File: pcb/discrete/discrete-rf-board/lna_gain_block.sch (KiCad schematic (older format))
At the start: 21 parts, among them Q801 Q_NPN_BCEE

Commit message: The footprintening continues
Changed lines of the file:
@@
 $Descr A4 11693 8268
 encoding utf-8
-Sheet 14 19
+Sheet 16 19
 Title ""
 Date ""
@@
 AR Path="/5CA6B0AA/5CE74EBE/5D4104E7/5D3CF638" Ref="R903"  Part="1"
 AR Path="/5CA6B0AA/5CE74EBE/5D4124AC/5D3CF638" Ref="R1003"  Part="1"
-F 0 "R803" H 6041 3404 50  0000 R CNN
+F 0 "R1003" H 6041 3404 50  0000 R CNN
 F 1 "75R" H 6041 3495 50  0000 R CNN
 F 2 "" H 6100 3450 50  0001 C CNN
@@
 AR Path="/5CA6B0AA/5CE74EBE/5D4104E7/5D3CF640" Ref="C910"  Part="1"
 AR Path="/5CA6B0AA/5CE74EBE/5D4124AC/5D3CF640" Ref="C1010"  Part="1"
-F 0 "C810" V 7129 3250 50  0000 C CNN
+F 0 "C1010" V 7129 3250 50  0000 C CNN
 F 1 "100 pF RF" V 7038 3250 50  0000 C CNN
 F 2 "" H 6900 3250 50  0001 C CNN
@@
 AR Path="/5CA6B0AA/5CE74EBE/5D4104E7/5D3CF649" Ref="#PWR0903"  Part="1"
 AR Path="/5CA6B0AA/5CE74EBE/5D4124AC/5D3CF649" Ref="#PWR01003"  Part="1"
-F 0 "#PWR0803" H 4500 3800 50  0001 C CNN
+F 0 "#PWR01003" H 4500 3800 50  0001 C CNN
 F 1 "GND" H 4505 3877 50  0000 C CNN
 F 2 "" H 4500 4050 50  0001 C CNN
@@
 AR Path="/5CA6B0AA/5CE74EBE/5D4104E7/5D3CF650" Ref="#PWR0910"  Part="1"
 AR Path="/5CA6B0AA/5CE74EBE/5D4124AC/5D3CF650" Ref="#PWR01010"  Part="1"
-F 0 "#PWR0810" H 6700 3550 50  0001 C CNN
+F 0 "#PWR01010" H 6700 3550 50  0001 C CNN
 F 1 "GND" H 6705 3627 50  0000 C CNN
 F 2 "" H 6700 3800 50  0001 C CNN
@@
 AR Path="/5CA6B0AA/5CE74EBE/5D4104E7/5D3CF659" Ref="R901"  Part="1"
 AR Path="/5CA6B0AA/5CE74EBE/5D4124AC/5D3CF659" Ref="R1001"  Part="1"
-F 0 "R801" H 4441 3354 50  0000 R CNN
+F 0 "R1001" H 4441 3354 50  0000 R CNN
 F 1 "8k2R" H 4441 3445 50  0000 R CNN
 F 2 "" H 4500 3400 50  0001 C CNN
@@
 AR Path="/5CA6B0AA/5CE74EBE/5D4104E7/5D3CF668" Ref="C909"  Part="1"
 AR Path="/5CA6B0AA/5CE74EBE/5D4124AC/5D3CF668" Ref="C1009"  Part="1"
-F 0 "C809" H 6792 3696 50  0000 L CNN
+F 0 "C1009" H 6792 3696 50  0000 L CNN
 F 1 "3.0 pF RF" H 6792 3605 50  0000 L CNN
 F 2 "" H 6700 3650 50  0001 C CNN
@@
 AR Path="/5CA6B0AA/5CE74EBE/5D4104E7/5D3CF670" Ref="L903"  Part="1"
 AR Path="/5CA6B0AA/5CE74EBE/5D4124AC/5D3CF670" Ref="L1003"  Part="1"
-F 0 "L803" V 6485 3250 50  0000 C CNN
+F 0 "L1003" V 6485 3250 50  0000 C CNN
 F 1 "10.0 nH" V 6394 3250 50  0000 C CNN
 F 2 "" H 6300 3250 50  0001 C CNN
@@
 AR Path="/5CA6B0AA/5CE74EBE/5D4104E7/5D3CF693" Ref="C902"  Part="1"
 AR Path="/5CA6B0AA/5CE74EBE/5D4124AC/5D3CF693" Ref="C1002"  Part="1"
-F 0 "C802" V 4529 3700 50  0000 C CNN
+F 0 "C1002" V 4529 3700 50  0000 C CNN
 F 1 "100 pF RF" V 4438 3700 50  0000 C CNN
 F 2 "" H 4300 3700 50  0001 C CNN
@@
 AR Path="/5CA6B0AA/5CE74EBE/5D4104E7/5D3CF699" Ref="L901"  Part="1"
 AR Path="/5CA6B0AA/5CE74EBE/5D4124AC/5D3CF699" Ref="L1001"  Part="1"
-F 0 "L801" V 4885 3700 50  0000 C CNN
+F 0 "L1001" V 4885 3700 50  0000 C CNN
 F 1 "9.5 nH" V 4794 3700 50  0000 C CNN
 F 2 "" H 4700 3700 50  0001 C CNN
@@
 AR Path="/5CA6B0AA/5CE74EBE/5D4104E7/5D3CF69F" Ref="C904"  Part="1"
 AR Path="/5CA6B0AA/5CE74EBE/5D4124AC/5D3CF69F" Ref="C1004"  Part="1"
-F 0 "C804" H 4592 3946 50  0000 L CNN
+F 0 "C1004" H 4592 3946 50  0000 L CNN
 F 1 "5.45 pF RF" H 4592 3855 50  0000 L CNN
 F 2 "" H 4500 3900 50  0001 C CNN
@@
 AR Path="/5CA6B0AA/5CE74EBE/5D4104E7/5D3CF6A6" Ref="#PWR0909"  Part="1"
 AR Path="/5CA6B0AA/5CE74EBE/5D4124AC/5D3CF6A6" Ref="#PWR01009"  Part="1"
-F 0 "#PWR0809" H 5550 3950 50  0001 C CNN
+F 0 "#PWR01009" H 5550 3950 50  0001 C CNN
 F 1 "GND" H 5555 4027 50  0000 C CNN
 F 2 "" H 5550 4200 50  0001 C CNN
@@
 AR Path="/5CA6B0AA/5CE74EBE/5D4104E7/5D3E5B01" Ref="C903"  Part="1"
 AR Path="/5CA6B0AA/5CE74EBE/5D4124AC/5D3E5B01" Ref="C1003"  Part="1"
-F 0 "C803" H 4410 2620 50  0000 L CNN
+F 0 "C1003" H 4410 2620 50  0000 L CNN
 F 1 "1 nF" H 4410 2470 50  0000 L CNN
 F 2 "" H 4400 2550 50  0001 C CNN
@@
 AR Path="/5CA6B0AA/5CE74EBE/5D4104E7/5D3E5B07" Ref="C906"  Part="1"
 AR Path="/5CA6B0AA/5CE74EBE/5D4124AC/5D3E5B07" Ref="C1006"  Part="1"
-F 0 "C806" H 4810 2620 50  0000 L CNN
+F 0 "C1006" H 4810 2620 50  0000 L CNN
 F 1 "100 pF RF" H 4810 2470 50  0000 L CNN
 F 2 "" H 4800 2550 50  0001 C CNN
@@
 AR Path="/5CA6B0AA/5CE74EBE/5D4104E7/5D3E5B0D" Ref="C908"  Part="1"
 AR Path="/5CA6B0AA/5CE74EBE/5D4124AC/5D3E5B0D" Ref="C1008"  Part="1"
-F 0 "C808" H 5210 2620 50  0000 L CNN
+F 0 "C1008" H 5210 2620 50  0000 L CNN
 F 1 "100 pF RF" H 5210 2470 50  0000 L CNN
 F 2 "" H 5200 2550 50  0001 C CNN
@@
 AR Path="/5CA6B0AA/5CE74EBE/5D4104E7/5D3E5B13" Ref="#PWR0902"  Part="1"
 AR Path="/5CA6B0AA/5CE74EBE/5D4124AC/5D3E5B13" Ref="#PWR01002"  Part="1"
-F 0 "#PWR0802" H 4400 2500 50  0001 C CNN
+F 0 "#PWR01002" H 4400 2500 50  0001 C CNN
 F 1 "GND" H 4400 2600 50  0000 C CNN
 F 2 "" H 4400 2750 50  0001 C CNN
@@
 AR Path="/5CA6B0AA/5CE74EBE/5D4104E7/5D3E5B19" Ref="#PWR0905"  Part="1"
 AR Path="/5CA6B0AA/5CE74EBE/5D4124AC/5D3E5B19" Ref="#PWR01005"  Part="1"
-F 0 "#PWR0805" H 4800 2500 50  0001 C CNN
+F 0 "#PWR01005" H 4800 2500 50  0001 C CNN
 F 1 "GND" H 4800 2600 50  0000 C CNN
 F 2 "" H 4800 2750 50  0001 C CNN
@@
 AR Path="/5CA6B0AA/5CE74EBE/5D4104E7/5D3E5B1F" Ref="#PWR0908"  Part="1"
 AR Path="/5CA6B0AA/5CE74EBE/5D4124AC/5D3E5B1F" Ref="#PWR01008"  Part="1"
-F 0 "#PWR0808" H 5200 2500 50  0001 C CNN
+F 0 "#PWR01008" H 5200 2500 50  0001 C CNN
 F 1 "GND" H 5200 2600 50  0000 C CNN
 F 2 "" H 5200 2750 50  0001 C CNN
@@
 AR Path="/5CA6B0AA/5CE74EBE/5D4104E7/5D3E5B25" Ref="C907"  Part="1"
 AR Path="/5CA6B0AA/5CE74EBE/5D4124AC/5D3E5B25" Ref="C1007"  Part="1"
-F 0 "C807" H 5160 1920 50  0000 L CNN
+F 0 "C1007" H 5160 1920 50  0000 L CNN
 F 1 "100 pF RF" H 5160 1770 50  0000 L CNN
 F 2 "" H 5150 1850 50  0001 C CNN
@@
 AR Path="/5CA6B0AA/5CE74EBE/5D4104E7/5D3E5B2B" Ref="#PWR0907"  Part="1"
 AR Path="/5CA6B0AA/5CE74EBE/5D4124AC/5D3E5B2B" Ref="#PWR01007"  Part="1"
-F 0 "#PWR0807" H 5150 1800 50  0001 C CNN
+F 0 "#PWR01007" H 5150 1800 50  0001 C CNN
 F 1 "GND" H 5150 1900 50  0000 C CNN
 F 2 "" H 5150 2050 50  0001 C CNN
@@
 AR Path="/5CA6B0AA/5CE74EBE/5D4104E7/5D3E5B31" Ref="C905"  Part="1"
 AR Path="/5CA6B0AA/5CE74EBE/5D4124AC/5D3E5B31" Ref="C1005"  Part="1"
-F 0 "C805" H 4760 1920 50  0000 L CNN
+F 0 "C1005" H 4760 1920 50  0000 L CNN
 F 1 "1 nF" H 4760 1770 50  0000 L CNN
 F 2 "" H 4750 1850 50  0001 C CNN
@@
 AR Path="/5CA6B0AA/5CE74EBE/5D4104E7/5D3E5B37" Ref="#PWR0904"  Part="1"
 AR Path="/5CA6B0AA/5CE74EBE/5D4124AC/5D3E5B37" Ref="#PWR01004"  Part="1"
-F 0 "#PWR0804" H 4750 1800 50  0001 C CNN
+F 0 "#PWR01004" H 4750 1800 50  0001 C CNN
 F 1 "GND" H 4750 1900 50  0000 C CNN
 F 2 "" H 4750 2050 50  0001 C CNN
@@
 AR Path="/5CA6B0AA/5CE74EBE/5D4104E7/5D3F1C48" Ref="R904"  Part="1"
 AR Path="/5CA6B0AA/5CE74EBE/5D4124AC/5D3F1C48" Ref="R1004"  Part="1"
-F 0 "R804" H 5580 2120 50  0000 L CNN
+F 0 "R1004" H 5580 2120 50  0000 L CNN
 F 1 "22R" H 5580 2060 50  0000 L CNN
 F 2 "" H 5550 2100 50  0001 C CNN
@@
 AR Path="/5CA6B0AA/5CE74EBE/5D4104E7/5D3FEB6E" Ref="C901"  Part="1"
 AR Path="/5CA6B0AA/5CE74EBE/5D4124AC/5D3FEB6E" Ref="C1001"  Part="1"
-F 0 "C801" H 4010 2620 50  0000 L CNN
+F 0 "C1001" H 4010 2620 50  0000 L CNN
 F 1 "1 nF" H 4010 2470 50  0000 L CNN
 F 2 "" H 4000 2550 50  0001 C CNN
@@
 AR Path="/5CA6B0AA/5CE74EBE/5D4104E7/5D3FEB74" Ref="#PWR0901"  Part="1"
 AR Path="/5CA6B0AA/5CE74EBE/5D4124AC/5D3FEB74" Ref="#PWR01001"  Part="1"
-F 0 "#PWR0801" H 4000 2500 50  0001 C CNN
+F 0 "#PWR01001" H 4000 2500 50  0001 C CNN
 F 1 "GND" H 4000 2600 50  0000 C CNN
 F 2 "" H 4000 2750 50  0001 C CNN
@@
 AR Path="/5CA6B0AA/5CE74EBE/5D4104E7/5D40D244" Ref="L902"  Part="1"
 AR Path="/5CA6B0AA/5CE74EBE/5D4124AC/5D40D244" Ref="L1002"  Part="1"
-F 0 "L802" H 5580 3090 50  0000 L CNN
+F 0 "L1002" H 5580 3090 50  0000 L CNN
 F 1 "220 nH" H 5580 3010 50  0000 L CNN
 F 2 "" H 5550 3050 50  0001 C CNN
@@
 AR Path="/5CA6B0AA/5CE74EBE/5D4104E7/5D435867" Ref="R902"  Part="1"
 AR Path="/5CA6B0AA/5CE74EBE/5D4124AC/5D435867" Ref="R1002"  Part="1"
-F 0 "R802" H 4941 3254 50  0000 R CNN
+F 0 "R1002" H 4941 3254 50  0000 R CNN
 F 1 "1k8R" H 4941 3345 50  0000 R CNN
 F 2 "" H 5000 3300 50  0001 C CNN
@@
 AR Path="/5CA6B0AA/5CE74EBE/5D3C8D48/5D43681D" Ref="#PWR0806"  Part="1"
 AR Path="/5CA6B0AA/5CE74EBE/5D4104E7/5D43681D" Ref="#PWR0906"  Part="1"
-F 0 "#PWR0806" H 5000 3250 50  0001 C CNN
+F 0 "#PWR01006" H 5000 3250 50  0001 C CNN
 F 1 "GND" H 5000 3350 50  0000 C CNN
 F 2 "" H 5000 3500 50  0001 C CNN
@@
 AR Path="/5CA6B0AA/5CE74EBE/5D4104E7/5D191C23" Ref="Q901"  Part="1"
 AR Path="/5CA6B0AA/5CE74EBE/5D4124AC/5D191C23" Ref="Q1001"  Part="1"
-F 0 "Q801" H 5800 3700 50  0000 C CNN
+F 0 "Q1001" H 5800 3700 50  0000 C CNN
 F 1 "Q_NPN_BCEE" H 5700 3600 50  0000 L CNN
 F 2 "" H 5500 3700 50  0001 C CNN

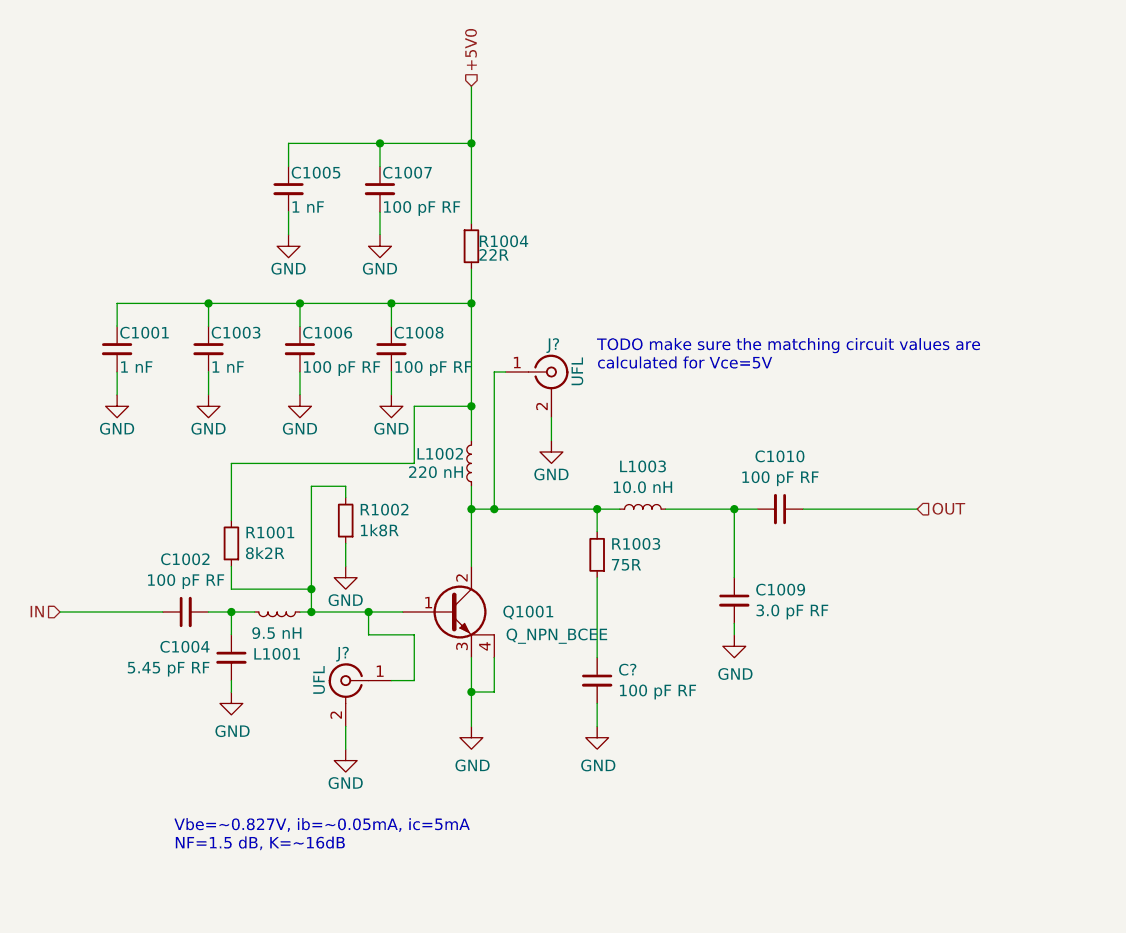
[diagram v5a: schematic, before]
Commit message: Add matching PNP/NPN transistor pairs, fix pin numbering for BFU520R transistors TODO fix biasing on power stage, source last NPN transistor, autofill and start sourcing passives
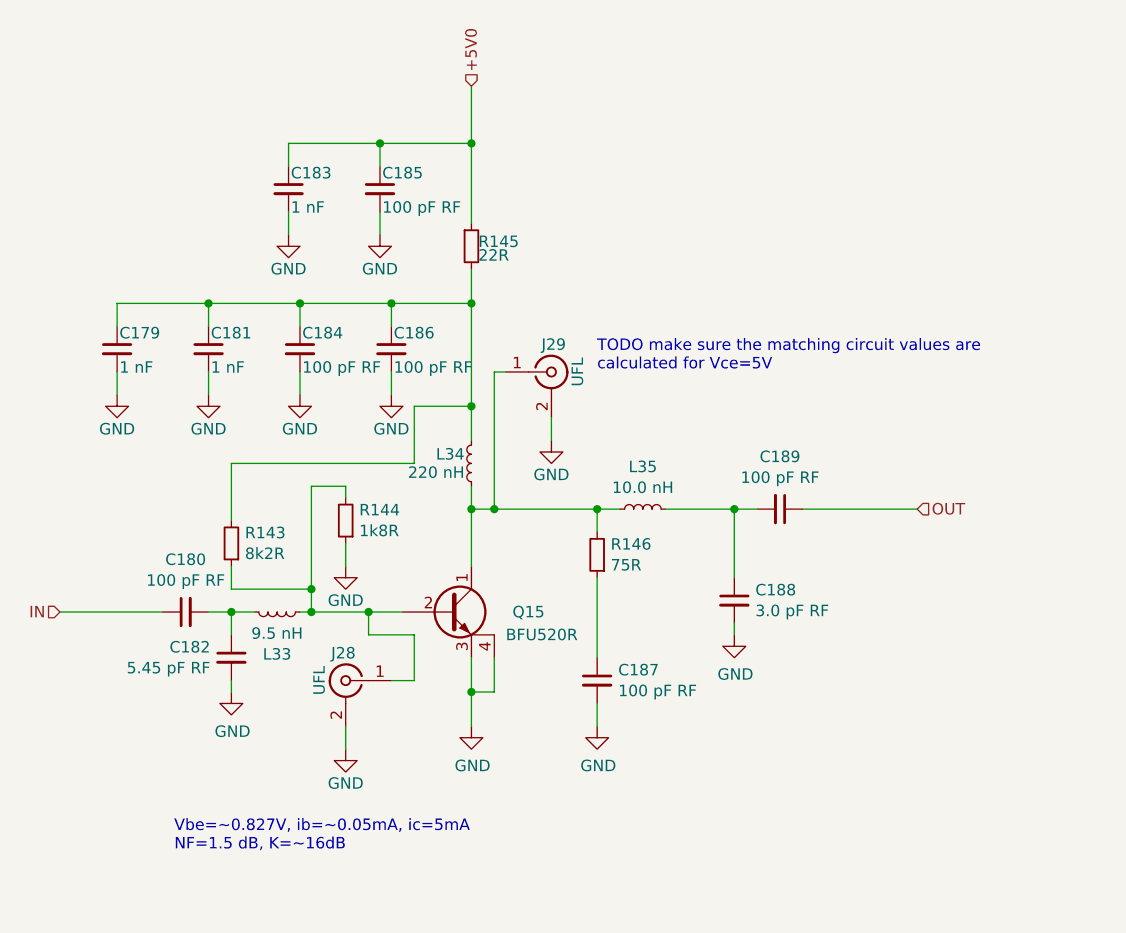
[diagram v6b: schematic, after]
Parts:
- removed Q801: Q_NPN_BCEE, symbol discrete-parts:Q_NPN_BCEE
- added Q15: BFU520R, symbol discrete-parts:Q_NPN_CBEE
- gave numbers to parts that had none: 3
- renumbered C801 to C157, C802 to C158, C803 to C159, C804 to C160, C805 to C161, C806 to C162, C807 to C163, C808 to C164, C809 to C166, C810 to C167, L801 to L27, L802 to L28, L803 to L29, R801 to R135, R802 to R136, R804 to R137, R803 to R138
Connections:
- net GND: now also Q15.3 (E), Q15.4 (C)
- net at J24.1 (In), L27.2, R135.1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: now also Q15.2 (B)
- net at J25.1 (In), L28.2, L29.1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: now also Q15.1 (C)

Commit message: All component values set (TODO change transistor gain stages to match values from experimentation
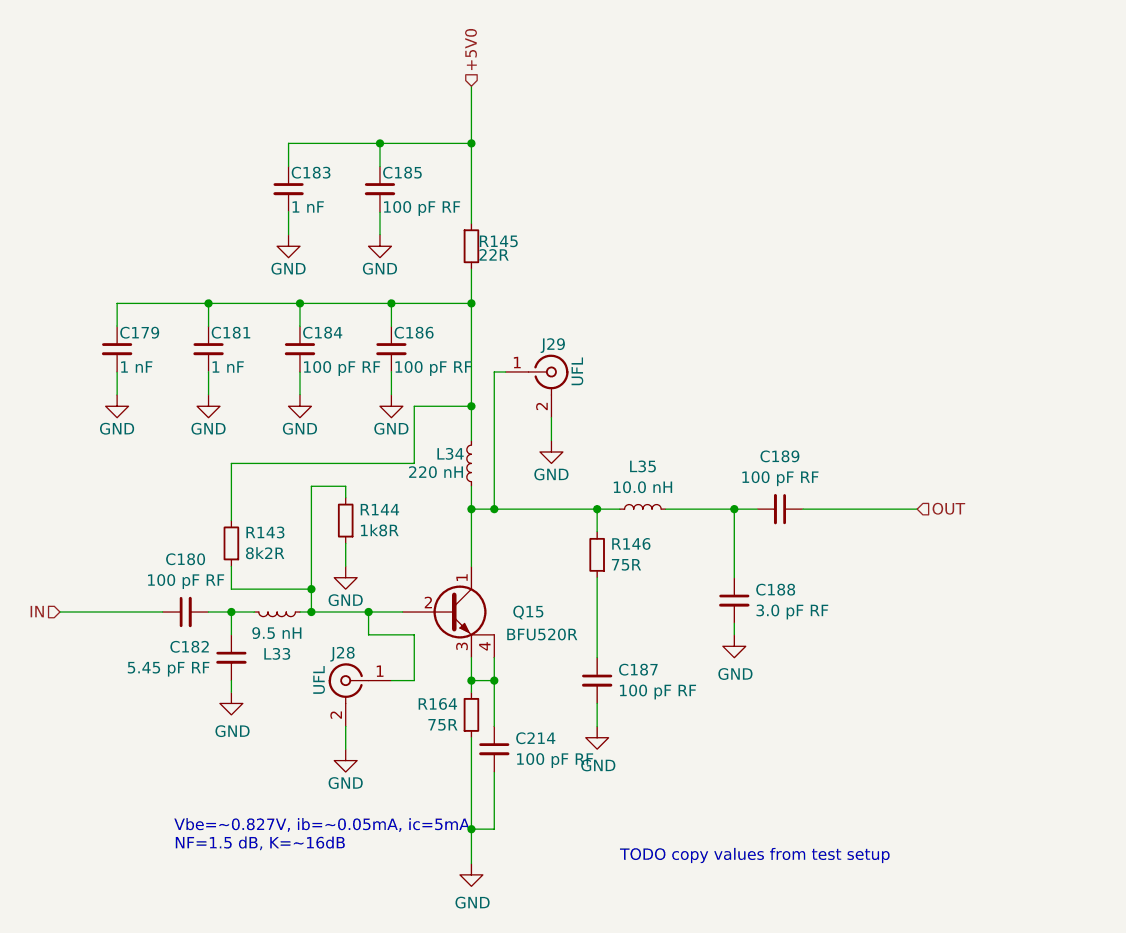
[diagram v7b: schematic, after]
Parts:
- added C212: 100 pF RF, symbol Device:C_Small
- added R162: 75R, symbol Device:R_Small
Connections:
- net GND: now also C212.2, R162.1; no longer Q15.3 (E), Q15.4 (C)
- new net: C212.1, Q15.3 (E), Q15.4 (C), R162.2
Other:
- note added: "TODO copy values from test setup"
- note removed: "TODO make sure the matching circuit values are\ncalculated for Vce=5V"
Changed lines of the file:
@@
 L power:GND #PWR?
 U 1 1 5D3CF6A6
-P 5550 4200
+P 5550 4800
 AR Path="/5CA6B0AA/5CE74EBE/5D3CF6A6" Ref="#PWR?"  Part="1"
 AR Path="/5CA6B0AA/5CE74EBE/5D3C8D48/5D3CF6A6" Ref="#PWR0208"  Part="1"
@@
 AR Path="/5CA6B0AA/5CE74EBE/5D4104E7/5D3CF6A6" Ref="#PWR0221"  Part="1"
 AR Path="/5CA6B0AA/5CE74EBE/5D4124AC/5D3CF6A6" Ref="#PWR0234"  Part="1"
-F 0 "#PWR0234" H 5550 3950 50  0001 C CNN
-F 1 "GND" H 5555 4027 50  0000 C CNN
-F 2 "" H 5550 4200 50  0001 C CNN
-F 3 "" H 5550 4200 50  0001 C CNN
-	1    5550 4200
+F 0 "#PWR0234" H 5550 4550 50  0001 C CNN
+F 1 "GND" H 5555 4627 50  0000 C CNN
+F 2 "" H 5550 4800 50  0001 C CNN
+F 3 "" H 5550 4800 50  0001 C CNN
+	1    5550 4800
 	1    0    0    -1
 $EndComp
@@
 	5000 3150 5000 3200
 Wire Wire Line
-	5550 3900 5550 4050
-Wire Wire Line
-	5650 3900 5650 4050
-Wire Wire Line
-	5650 4050 5550 4050
-Connection ~ 5550 4050
-Wire Wire Line
-	5550 4050 5550 4200
+	5650 4650 5550 4650
+Connection ~ 5550 4650
+Wire Wire Line
+	5550 4650 5550 4800
 Text Notes 4250 4750 0    50   ~ 0
 Vbe=~~0.827V, ib=~~0.05mA, ic=5mA\nNF=1.5 dB, K=~~16dB
-Text Notes 6100 2650 0    50   ~ 0
-TODO make sure the matching circuit values are\ncalculated for Vce=5V
 $Comp
 L Device:C_Small C?
@@
 	1    0    0    -1
 $EndComp
+Wire Wire Line
+	5550 3900 5550 4000
+Wire Wire Line
+	5550 4000 5650 4000
+Wire Wire Line
+	5650 4000 5650 3900
+$Comp
+L Device:C_Small C?
+U 1 1 5DAA0359
+P 5650 4300
+AR Path="/5CA6B0AA/5CE74EBE/5DAA0359" Ref="C?"  Part="1"
+AR Path="/5CA6B0AA/5CE74EBE/5D3C8D48/5DAA0359" Ref="C212"  Part="1"
+AR Path="/5CA6B0AA/5CE74EBE/5D407D69/5DAA0359" Ref="C?"  Part="1"
+AR Path="/5CA6B0AA/5CE74EBE/5D407DF5/5DAA0359" Ref="C?"  Part="1"
+AR Path="/5CA6B0AA/5CE74EBE/5D4104E7/5DAA0359" Ref="C213"  Part="1"
+AR Path="/5CA6B0AA/5CE74EBE/5D4124AC/5DAA0359" Ref="C214"  Part="1"
+F 0 "C214" H 5742 4346 50  0000 L CNN
+F 1 "100 pF RF" H 5742 4255 50  0000 L CNN
+F 2 "" H 5650 4300 50  0001 C CNN
+F 3 "~" H 5650 4300 50  0001 C CNN
+	1    5650 4300
+	1    0    0    -1
+$EndComp
+Wire Wire Line
+	5650 4400 5650 4650
+Wire Wire Line
+	5650 4200 5650 4000
+Connection ~ 5650 4000
+$Comp
+L Device:R_Small R?
+U 1 1 5DAA3BBB
+P 5550 4150
+AR Path="/5CA6B0AA/5CE74EBE/5DAA3BBB" Ref="R?"  Part="1"
+AR Path="/5CA6B0AA/5CE74EBE/5D3C8D48/5DAA3BBB" Ref="R162"  Part="1"
+AR Path="/5CA6B0AA/5CE74EBE/5D407D69/5DAA3BBB" Ref="R?"  Part="1"
+AR Path="/5CA6B0AA/5CE74EBE/5D407DF5/5DAA3BBB" Ref="R?"  Part="1"
+AR Path="/5CA6B0AA/5CE74EBE/5D4104E7/5DAA3BBB" Ref="R163"  Part="1"
+AR Path="/5CA6B0AA/5CE74EBE/5D4124AC/5DAA3BBB" Ref="R164"  Part="1"
+F 0 "R164" H 5491 4104 50  0000 R CNN
+F 1 "75R" H 5491 4195 50  0000 R CNN
+F 2 "" H 5550 4150 50  0001 C CNN
+F 3 "~" H 5550 4150 50  0001 C CNN
+	1    5550 4150
+	1    0    0    1
+$EndComp
+Wire Wire Line
+	5550 4250 5550 4650
+Wire Wire Line
+	5550 4050 5550 4000
+Connection ~ 5550 4000
+Text Notes 6200 4800 0    50   ~ 0
+TODO copy values from test setup
 $EndSCHEMATC

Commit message: Autofill; lots left to do
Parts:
- J24, J25: footprint (none) -> discrete_footprints:2337019-1; Mouser (none) -> 571-2337019-1
- Q15: footprint (none) -> discrete_footprints:NXP_SOT143B; Mouser (none) -> 771-BFU520R
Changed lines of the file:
@@
 F 0 "J29" H 5910 2770 50  0000 C CNN
 F 1 "UFL" V 6015 2650 50  0000 C CNN
-F 2 "" H 5900 2650 50  0001 C CNN
+F 2 "discrete_footprints:2337019-1" H 5900 2650 50  0001 C CNN
 F 3 " ~" H 5900 2650 50  0001 C CNN
+F 4 " 571-2337019-1" H 5900 2650 50  0001 C CNN "Mouser"
 	1    5900 2650
 	1    0    0    -1
@@
 F 0 "J28" H 5010 4120 50  0000 C CNN
 F 1 "UFL" V 5115 4000 50  0000 C CNN
-F 2 "" H 5000 4000 50  0001 C CNN
+F 2 "discrete_footprints:2337019-1" H 5000 4000 50  0001 C CNN
 F 3 " ~" H 5000 4000 50  0001 C CNN
+F 4 " 571-2337019-1" H 5000 4000 50  0001 C CNN "Mouser"
 	1    5000 4000
 	-1   0    0    -1
@@
 F 0 "Q15" H 5800 3700 50  0000 C CNN
 F 1 "BFU520R" H 5700 3600 50  0000 L CNN
-F 2 "" H 5500 3700 50  0001 C CNN
+F 2 "discrete_footprints:NXP_SOT143B" H 5500 3700 50  0001 C CNN
 F 3 "" H 5500 3700 50  0001 C CNN
+F 4 " 771-BFU520R " H 5500 3700 50  0001 C CNN "Mouser"
 	1    5500 3700
 	1    0    0    -1
